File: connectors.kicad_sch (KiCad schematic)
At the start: 46 parts, among them J6 10107844-002LF, J7 PinHeader_1x4_P2.5mm_Drill1mm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, J8 JST_XH_1x2_S2B-XH-A-LF-SN, J9 PinHeader_1x2_P2.5mm_Drill1mm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, SW1 MSS3-V-T_R, U11 USB-C_GCT_USB4145-03-0070-C

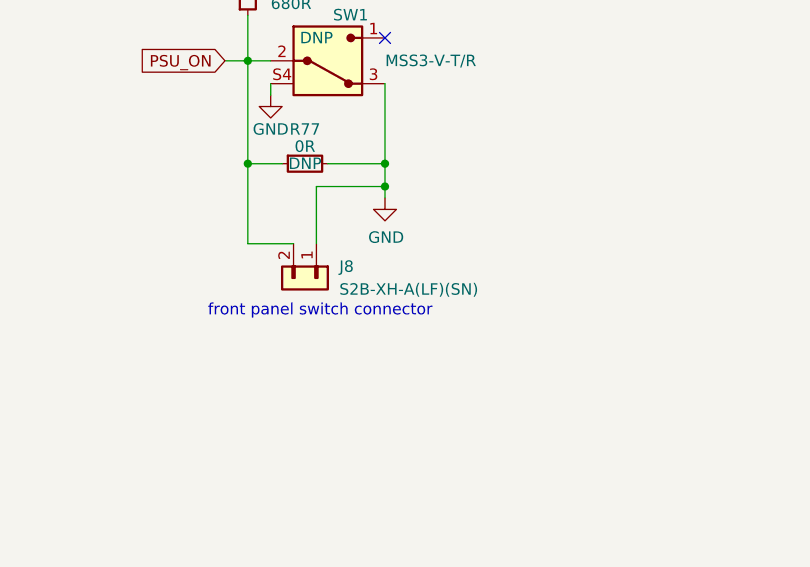
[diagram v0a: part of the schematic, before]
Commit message: Replace power switch connector
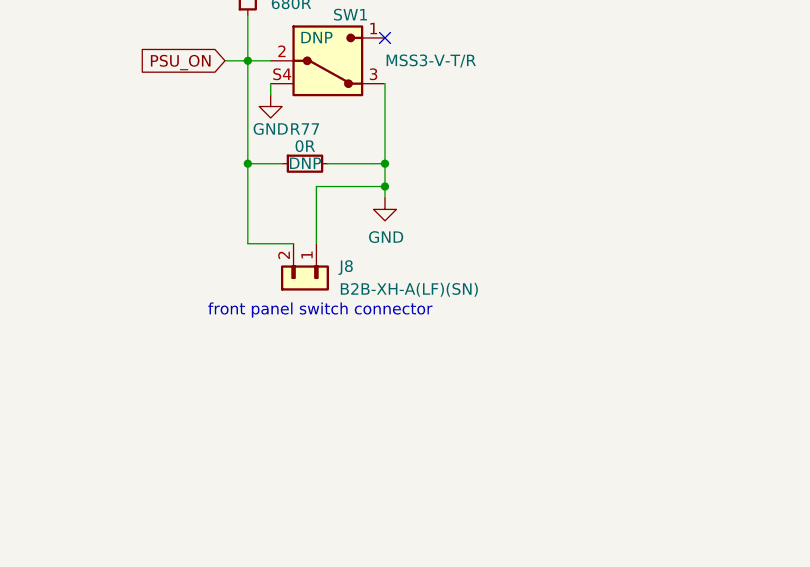
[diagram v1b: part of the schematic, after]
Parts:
- removed J8: JST_XH_1x2_S2B-XH-A-LF-SN, antmicro-footprints:Conn_JST_XH_1x2_S2B-XH-A-LF-SN, symbol antmicroWire2BoardConnectors:JST_XH_1x2_S2B-XH-A-LF-SN
- added J8: JST_XH_1x2_B2B-XH-A-LF-SN, antmicro-footprints:Conn_JST_XH_1x2_B2B-XH-A-LF-SN, symbol antmicroWire2BoardConnectors:JST_XH_1x2_B2B-XH-A-LF-SN
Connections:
- net GND: now also J8.1
- net PSU_ON: now also J8.2
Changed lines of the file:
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@@
     (pin "1")
+  )
+  (symbol (lib_id "antmicroWire2BoardConnectors:JST_XH_1x2_B2B-XH-A-LF-SN") (at 198.12 152.4 270) (unit 1)
+    (in_bom yes) (on_board yes) (fields_autoplaced)
+    (property "Reference" "J8" (id 0) (at 200.66 154.9399 90)
+      (effects (font (size 1.27 1.27) (thickness 0.15)) (justify left))
+    )
+    (property "Value" "JST_XH_1x2_B2B-XH-A-LF-SN" (id 1) (at 196.85 160.02 0)
+      (effects (font (size 1.27 1.27) (thickness 0.15)) (justify left bottom) hide)
+    )
+    (property "Footprint" "antmicro-footprints:Conn_JST_XH_1x2_B2B-XH-A-LF-SN" (id 2) (at 194.31 160.02 0)
+      (effects (font (size 1.27 1.27) (thickness 0.15)) (justify left bottom) hide)
+    )
+    (property "Datasheet" "http://www.jst-mfg.com/product/pdf/eng/eXH.pdf" (id 3) (at 191.77 160.02 0)
+      (effects (font (size 1.27 1.27) (thickness 0.15)) (justify left bottom) hide)
+    )
+    (property "MPN" "B2B-XH-A(LF)(SN)" (id 4) (at 200.66 157.4799 90)
+      (effects (font (size 1.27 1.27) (thickness 0.15)) (justify left))
+    )
+    (property "Manufacturer" "JST Automotive Connectors" (id 5) (at 186.69 160.02 0)
+      (effects (font (size 1.27 1.27) (thickness 0.15)) (justify left bottom) hide)
+    )
+    (property "Author" "Antmicro" (id 6) (at 184.15 160.02 0)
+      (effects (font (size 1.27 1.27) (thickness 0.15)) (justify left bottom) hide)
+    )
+    (property "License" "Apache-2.0" (id 7) (at 181.61 160.02 0)
+      (effects (font (size 1.27 1.27) (thickness 0.15)) (justify left bottom) hide)
+    )
+    (pin "1")
+    (pin "2")
   )
   (symbol (lib_name "1N4148WS-7-F_1") (lib_id "antmicroDiodesRectifiersSingle:1N4148WS-7-F") (at 210.82 223.52 90) (unit 1)
@@
     (pin "1")
   )
-  (symbol (lib_id "antmicroWire2BoardConnectors:JST_XH_1x2_S2B-XH-A-LF-SN") (at 198.12 152.4 270) (unit 1)
-    (in_bom yes) (on_board yes) (fields_autoplaced)
-    (property "Reference" "J8" (id 0) (at 200.66 154.9399 90)
-      (effects (font (size 1.27 1.27) (thickness 0.15)) (justify left))
-    )
-    (property "Value" "JST_XH_1x2_S2B-XH-A-LF-SN" (id 1) (at 187.96 177.8 0)
-      (effects (font (size 1.27 1.27) (thickness 0.15)) (justify left bottom) hide)
-    )
-    (property "Footprint" "antmicro-footprints:Conn_JST_XH_1x2_S2B-XH-A-LF-SN" (id 2) (at 185.42 177.8 0)
-      (effects (font (size 1.27 1.27) (thickness 0.15)) (justify left bottom) hide)
-    )
-    (property "Datasheet" "https://www.tme.eu/Document/0a99312bb6c67d3f0f7869fe9a023cea/XH.pdf" (id 3) (at 182.88 177.8 0)
-      (effects (font (size 1.27 1.27) (thickness 0.15)) (justify left bottom) hide)
-    )
-    (property "MPN" "S2B-XH-A(LF)(SN)" (id 4) (at 200.66 157.4799 90)
-      (effects (font (size 1.27 1.27) (thickness 0.15)) (justify left))
-    )
-    (property "Manufacturer" "JST Automotive Connectors" (id 5) (at 190.5 177.8 0)
-      (effects (font (size 1.27 1.27) (thickness 0.15)) (justify left bottom) hide)
-    )
-    (property "Author" "Antmicro" (id 6) (at 180.34 177.8 0)
-      (effects (font (size 1.27 1.27) (thickness 0.15)) (justify left bottom) hide)
-    )
-    (property "License" "Apache-2.0" (id 7) (at 177.8 177.8 0)
-      (effects (font (size 1.27 1.27) (thickness 0.15)) (justify left bottom) hide)
-    )
-    (pin "1")
-    (pin "2")
-  )
   (symbol (lib_id "antmicropower:GND") (at 321.31 162.56 0) (unit 1)

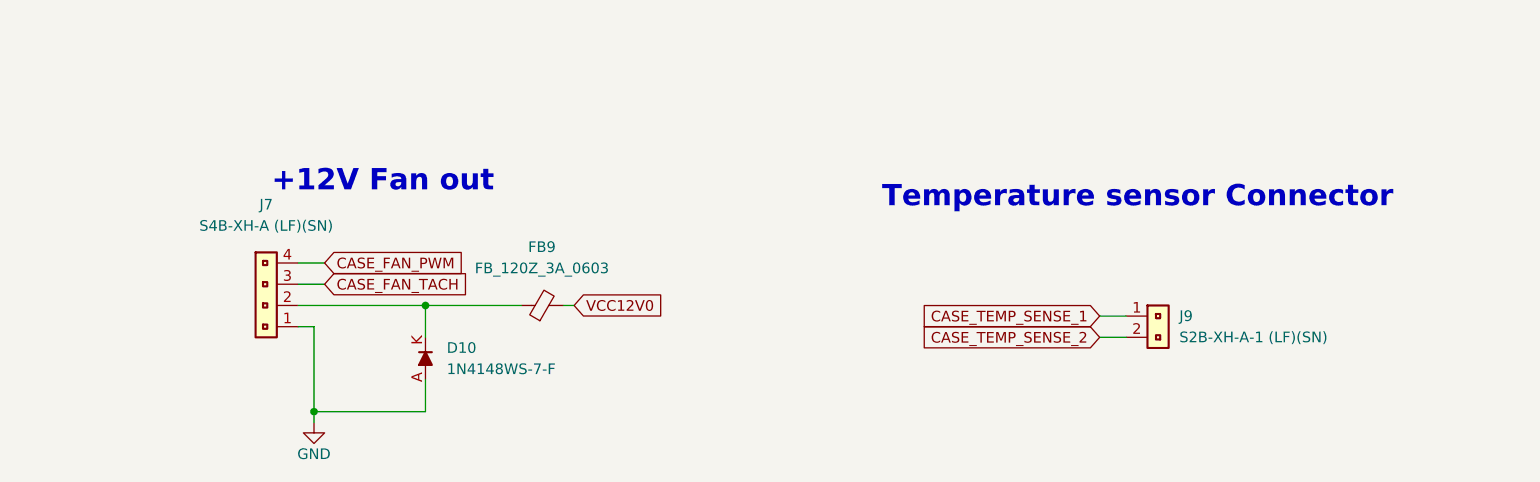
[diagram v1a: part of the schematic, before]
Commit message: Replace connectord with standard alternatives
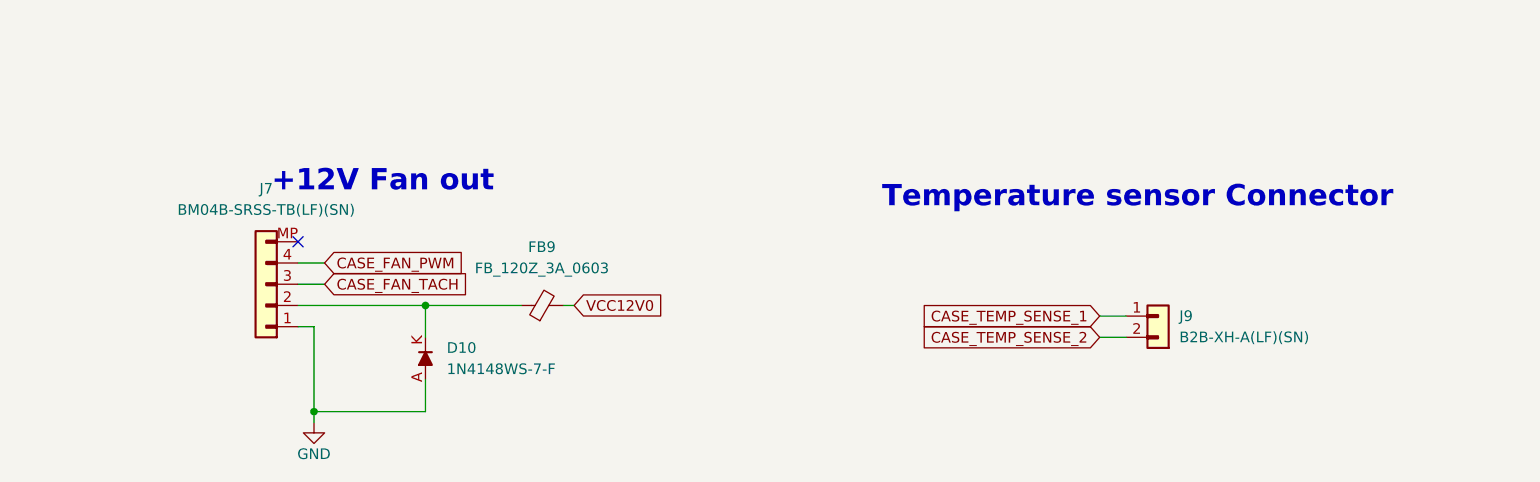
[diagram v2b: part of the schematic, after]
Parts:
- removed J7: PinHeader_1x4_P2.5mm_Drill1mm_Horizontal_Shrouded, antmicro-footprints:PinHeader_1x4_P2.5mm_Drill1mm_Horizontal_Shrouded, symbol antmicroRectangularConnectorsHeadersMalePins:PinHeader_1x4_P2.5mm_Drill1mm_Hori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
- removed J9: PinHeader_1x2_P2.5mm_Drill1mm_Horizontal_Shrouded, antmicro-footprints:PinHeader_1x2_P2.5mm_Drill1mm_Horizontal_Shrouded, symbol antmicroRectangularConnectorsHeadersMalePins:PinHeader_1x2_P2.5mm_Drill1mm_Hori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
- added J7: JST_SH_1x4_BM04B-SRSS-TB-LF-SN, antmicro-footprints:Conn_JST_SH_1x4_BM04B-SRSS-TB-LF-SN, symbol antmicroWire2BoardConnectors:JST_SH_1x4_BM04B-SRSS-TB-LF-SN
- added J9: JST_XH_1x2_B2B-XH-A-LF-SN, antmicro-footprints:Conn_JST_XH_1x2_B2B-XH-A-LF-SN, symbol antmicroWire2BoardConnectors:JST_XH_1x2_B2B-XH-A-LF-SN
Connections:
- net CASE_FAN_PWM: now also J7.4 (Pin_4)
- net CASE_FAN_TACH: now also J7.3 (Pin_3)
- net CASE_TEMP_SENSE_1: now also J9.1
- net CASE_TEMP_SENSE_2: now also J9.2
- net GND: now also J7.1 (Pin_1)
- net at D10.K, FB9.1: now also J7.2 (Pin_2)
- no-connect marks 1 -> 2
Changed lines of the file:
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@@
   )
   (no_connect (at 205.74 129.54))
+  (no_connect (at 195.58 207.01))
   (wire (pts (xy 78.74 102.87) (xy 78.74 105.41))
     (stroke (width 0) (type default) (color 0 0 0 0))
@@
     (pin "1")
   )
+  (symbol (lib_id "antmicroWire2BoardConnectors:JST_SH_1x4_BM04B-SRSS-TB-LF-SN") (at 195.58 217.17 180) (unit 1)
+    (in_bom yes) (on_board yes) (fields_autoplaced)
+    (property "Reference" "J7" (id 0) (at 191.77 200.66 0)
+      (effects (font (size 1.27 1.27) (thickness 0.15)))
+    )
+    (property "Value" "JST_SH_1x4_BM04B-SRSS-TB-LF-SN" (id 1) (at 175.26 209.55 0)
+      (effects (font (size 1.27 1.27) (thickness 0.15)) (justify left bottom) hide)
+    )
+    (property "Footprint" "antmicro-footprints:Conn_JST_SH_1x4_BM04B-SRSS-TB-LF-SN" (id 2) (at 175.26 207.01 0)
+      (effects (font (size 1.27 1.27) (thickness 0.15)) (justify left bottom) hide)
+    )
+    (property "Datasheet" "https://www.jst-mfg.com/product/pdf/eng/eSH.pdf" (id 3) (at 175.26 204.47 0)
+      (effects (font (size 1.27 1.27) (thickness 0.15)) (justify left bottom) hide)
+    )
+    (property "MPN" "BM04B-SRSS-TB(LF)(SN) " (id 4) (at 191.77 203.2 0)
+      (effects (font (size 1.27 1.27) (thickness 0.15)))
+    )
+    (property "Manufacturer" "JST Automotive Connectors" (id 5) (at 175.26 199.39 0)
+      (effects (font (size 1.27 1.27) (thickness 0.15)) (justify left bottom) hide)
+    )
+    (property "Author" "Antmicro" (id 6) (at 175.26 196.85 0)
+      (effects (font (size 1.27 1.27) (thickness 0.15)) (justify left bottom) hide)
+    )
+    (property "License" "Apache-2.0" (id 7) (at 175.26 194.31 0)
+      (effects (font (size 1.27 1.27) (thickness 0.15)) (justify left bottom) hide)
+    )
+    (pin "1")
+    (pin "2")
+    (pin "3")
+    (pin "4")
+    (pin "MP")
+  )
   (symbol (lib_id "antmicropower:GND") (at 373.38 144.78 0) (unit 1)
     (in_bom yes) (on_board yes)
@@
     (pin "1")
   )
-  (symbol (lib_id "antmicroRectangularConnectorsHeadersMalePins:PinHeader_1x4_P2.5mm_Drill1mm_Horizontal_Shrouded") (at 195.58 217.17 180) (unit 1)
-    (in_bom yes) (on_board yes) (fields_autoplaced)
-    (property "Reference" "J7" (id 0) (at 191.77 202.565 0)
-      (effects (font (size 1.27 1.27) (thickness 0.15)))
-    )
-    (property "Value" "PinHeader_1x4_P2.5mm_Drill1mm_Horizontal_Shrouded" (id 1) (at 170.18 209.55 0)
-      (effects (font (size 1.27 1.27) (thickness 0.15)) (justify left bottom) hide)
-    )
-    (property "Footprint" "antmicro-footprints:PinHeader_1x4_P2.5mm_Drill1mm_Horizontal_Shrouded" (id 2) (at 170.18 207.01 0)
-      (effects (font (size 1.27 1.27) (thickness 0.15)) (justify left bottom) hide)
-    )
-    (property "Datasheet" "https://www.tme.eu/Document/0a99312bb6c67d3f0f7869fe9a023cea/XH.pdf" (id 3) (at 170.18 204.47 0)
-      (effects (font (size 1.27 1.27) (thickness 0.15)) (justify left bottom) hide)
-    )
-    (property "MPN" "S4B-XH-A (LF)(SN)" (id 4) (at 191.77 205.105 0)
-      (effects (font (size 1.27 1.27) (thickness 0.15)))
-    )
-    (property "Manufacturer" "JST Automotive Connectors" (id 5) (at 170.18 201.93 0)
-      (effects (font (size 1.27 1.27) (thickness 0.15)) (justify left bottom) hide)
-    )
-    (property "Author" "Antmicro" (id 6) (at 170.18 199.39 0)
-      (effects (font (size 1.27 1.27) (thickness 0.15)) (justify left bottom) hide)
-    )
-    (property "License" "Apache-2.0" (id 7) (at 170.18 196.85 0)
-      (effects (font (size 1.27 1.27) (thickness 0.15)) (justify left bottom) hide)
-    )
-    (pin "1")
-    (pin "2")
-    (pin "3")
-    (pin "4")
-  )
   (symbol (lib_id "antmicroTestPoints:TP_1mm_SMD") (at 80.01 135.89 180) (unit 1)
     (in_bom yes) (on_board yes)
@@
     (pin "1")
   )
-  (symbol (lib_id "antmicroRectangularConnectorsHeadersMalePins:PinHeader_1x2_P2.5mm_Drill1mm_Horizontal_Shrouded") (at 294.64 215.9 0) (unit 1)
-    (in_bom yes) (on_board yes) (fields_autoplaced)
-    (property "Reference" "J9" (id 0) (at 300.99 215.8999 0)
-      (effects (font (size 1.27 1.27) (thickness 0.15)) (justify left))
-    )
-    (property "Value" "PinHeader_1x2_P2.5mm_Drill1mm_Horizontal_Shrouded" (id 1) (at 320.04 226.06 0)
-      (effects (font (size 1.27 1.27) (thickness 0.15)) (justify left bottom) hide)
-    )
-    (property "Footprint" "antmicro-footprints:PinHeader_1x2_P2.5mm_Drill1mm_Horizontal_Shrouded" (id 2) (at 320.04 228.6 0)
-      (effects (font (size 1.27 1.27) (thickness 0.15)) (justify left bottom) hide)
-    )
-    (property "Datasheet" "https://www.tme.eu/Document/0a99312bb6c67d3f0f7869fe9a023cea/XH.pdf" (id 3) (at 320.04 231.14 0)
-      (effects (font (size 1.27 1.27) (thickness 0.15)) (justify left bottom) hide)
-    )
-    (property "MPN" "S2B-XH-A-1 (LF)(SN)" (id 4) (at 300.99 218.4399 0)
-      (effects (font (size 1.27 1.27) (thickness 0.15)) (justify left))
-    )
-    (property "Manufacturer" "JST Automotive Connectors" (id 5) (at 320.04 223.52 0)
-      (effects (font (size 1.27 1.27) (thickness 0.15)) (justify left bottom) hide)
-    )
-    (property "Author" "Antmicro" (id 6) (at 320.04 233.68 0)
-      (effects (font (size 1.27 1.27) (thickness 0.15)) (justify left bottom) hide)
-    )
-    (property "License" "Apache-2.0" (id 7) (at 320.04 236.22 0)
-      (effects (font (size 1.27 1.27) (thickness 0.15)) (justify left bottom) hide)
-    )
-    (pin "1")
-    (pin "2")
-  )
   (symbol (lib_id "antmicroTestPoints:TP_1mm_SMD") (at 80.01 148.59 180) (unit 1)
     (in_bom yes) (on_board yes)
@@
     (pin "1")
   )
+  (symbol (lib_id "antmicroWire2BoardConnectors:JST_XH_1x2_B2B-XH-A-LF-SN") (at 294.64 215.9 0) (unit 1)
+    (in_bom yes) (on_board yes) (fields_autoplaced)
+    (property "Reference" "J9" (id 0) (at 300.99 215.8999 0)
+      (effects (font (size 1.27 1.27) (thickness 0.15)) (justify left))
+    )
+    (property "Value" "JST_XH_1x2_B2B-XH-A-LF-SN" (id 1) (at 302.26 217.17 0)
+      (effects (font (size 1.27 1.27) (thickness 0.15)) (justify left bottom) hide)
+    )
+    (property "Footprint" "antmicro-footprints:Conn_JST_XH_1x2_B2B-XH-A-LF-SN" (id 2) (at 302.26 219.71 0)
+      (effects (font (size 1.27 1.27) (thickness 0.15)) (justify left bottom) hide)
+    )
+    (property "Datasheet" "http://www.jst-mfg.com/product/pdf/eng/eXH.pdf" (id 3) (at 302.26 222.25 0)
+      (effects (font (size 1.27 1.27) (thickness 0.15)) (justify left bottom) hide)
+    )
+    (property "MPN" "B2B-XH-A(LF)(SN)" (id 4) (at 300.99 218.4399 0)
+      (effects (font (size 1.27 1.27) (thickness 0.15)) (justify left))
+    )
+    (property "Manufacturer" "JST Automotive Connectors" (id 5) (at 302.26 227.33 0)
+      (effects (font (size 1.27 1.27) (thickness 0.15)) (justify left bottom) hide)
+    )
+    (property "Author" "Antmicro" (id 6) (at 302.26 229.87 0)
+      (effects (font (size 1.27 1.27) (thickness 0.15)) (justify left bottom) hide)
+    )
+    (property "License" "Apache-2.0" (id 7) (at 302.26 232.41 0)
+      (effects (font (size 1.27 1.27) (thickness 0.15)) (justify left bottom) hide)
+    )
+    (pin "1")
+    (pin "2")
+  )
   (symbol (lib_id "antmicropower:GND") (at 193.04 135.89 0) (unit 1)

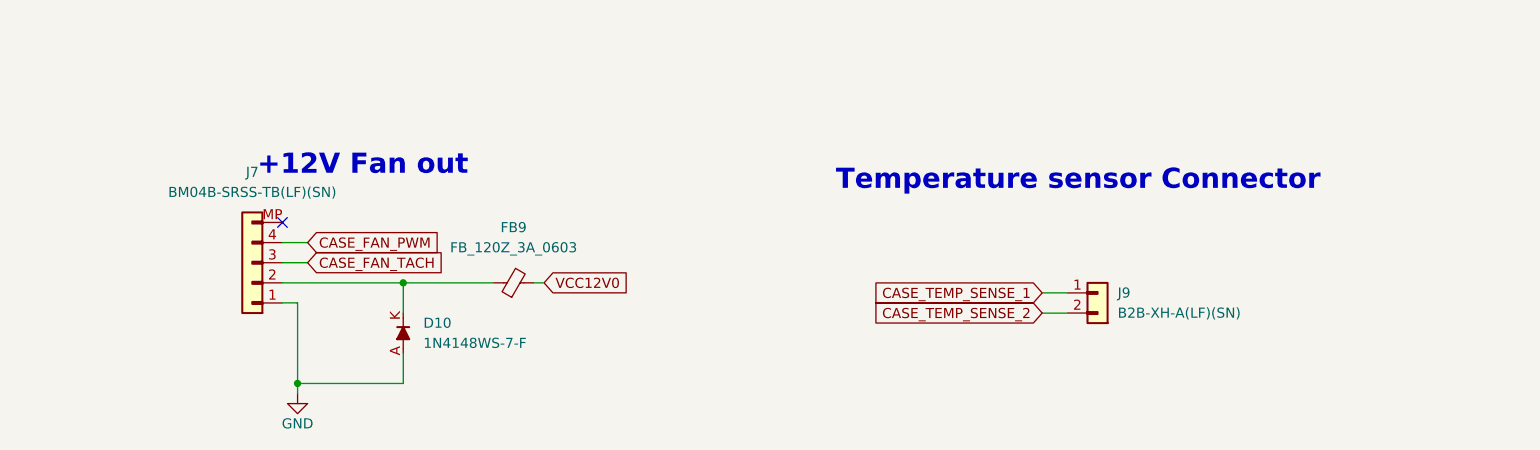
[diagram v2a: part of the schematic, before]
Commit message: Move internal fan to correct schematic sheet
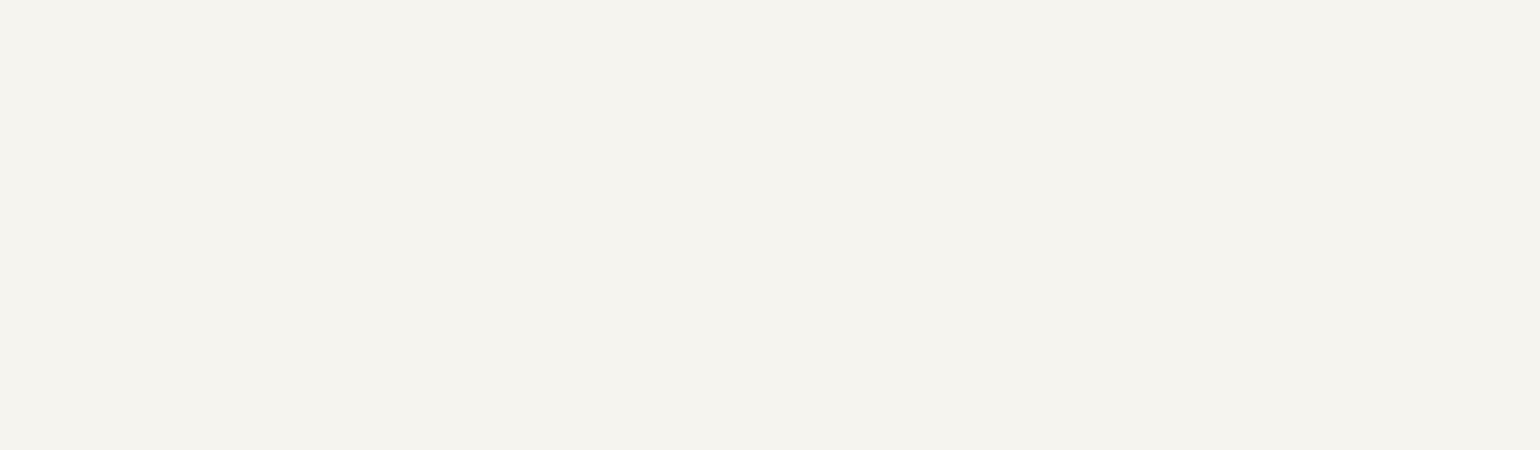
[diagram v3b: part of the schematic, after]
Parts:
- removed D10: 1N4148WS-7-F, antmicro-footprints:SOD-323, symbol antmicroDiodesRectifiersSingle:1N4148WS-7-F
- removed FB9: FB_120Z_3A_0603, antmicro-footprints:FB_0603_1608Metric, symbol antmicroFerriteBeadsandChips:FB_120Z_3A_0603
- removed J7: JST_SH_1x4_BM04B-SRSS-TB-LF-SN, antmicro-footprints:Conn_JST_SH_1x4_BM04B-SRSS-TB-LF-SN, symbol antmicroWire2BoardConnectors:JST_SH_1x4_BM04B-SRSS-TB-LF-SN
- removed J9: JST_XH_1x2_B2B-XH-A-LF-SN, antmicro-footprints:Conn_JST_XH_1x2_B2B-XH-A-LF-SN, symbol antmicroWire2BoardConnectors:JST_XH_1x2_B2B-XH-A-LF-SN
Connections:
- no-connect marks 2 -> 1
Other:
- note removed: "+12V Fan out"
- note removed: "Temperature sensor Connector"
